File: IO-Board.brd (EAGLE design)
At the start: 160 x 100 mm, 299 parts, among them IC1 PCF8574P, IC2 PCF8574P, IC3 PCF8574P, IC3_INT TPPAD1-13, IC4 PCF8574P, IC4_INT TPPAD1-13, J1.1 TPPAD1-13, J1.2 TPPAD1-13, J1.3 TPPAD1-13, J1.4 TPPAD1-13, J1.5 TPPAD1-13, J1.6 TPPAD1-13, J1.7 TPPAD1-13, J1.8 TPPAD1-13, J2.1 TPPAD1-13, J2.2 TPPAD1-13, J2.3 TPPAD1-13, J2.4 TPPAD1-13, J2.5 TPPAD1-13, J2.6 TPPAD1-13, J2.7 TPPAD1-13, J2.8 TPPAD1-13, J3.1 TPPAD1-13, J3.2 TPPAD1-13, J3.3 TPPAD1-13, J3.4 TPPAD1-13, J3.5 TPPAD1-13, J3.6 TPPAD1-13, J3.7 TPPAD1-13, J3.8 TPPAD1-13, J4.1 TPPAD1-13, J4.2 TPPAD1-13, J4.3 TPPAD1-13, J4.4 TPPAD1-13, J4.5 TPPAD1-13, J4.6 TPPAD1-13, J4.7 TPPAD1-13, J4.8 TPPAD1-13, J5 J7MM, T1 BC337-25, T10 BC337-25, T11 BC337-25, T12 BC337-25, T13 BC337-25, T14 BC337-25, T15 BC337-25, T16 BC337-25, T2 BC337-25, T3 BC337-25, T4 BC337-25, T5 BC337-25, T6 BC337-25, T7 BC337-25, T8 BC337-25, T9 BC337-25

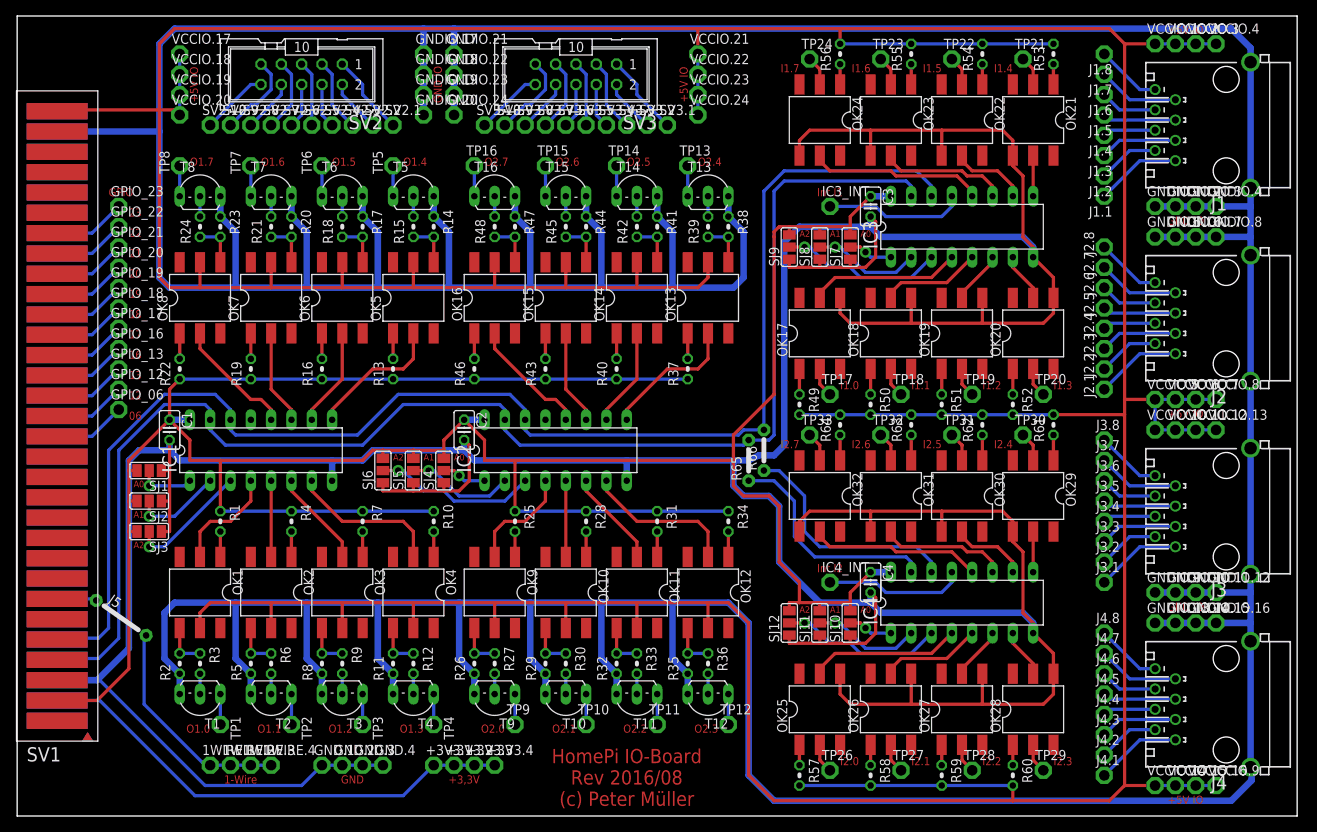
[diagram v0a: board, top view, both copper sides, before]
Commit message: IO-Board und IO-Board-2 Anpassungen
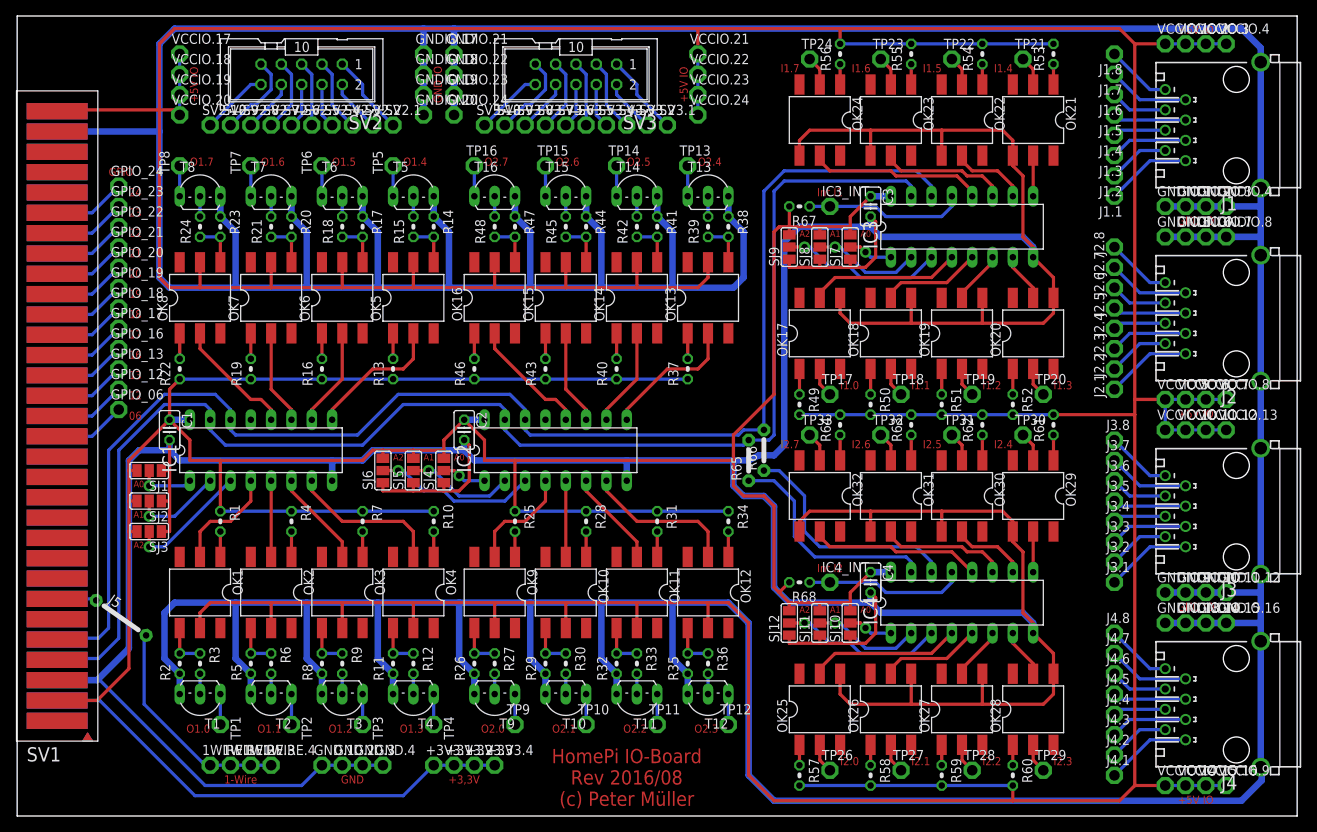
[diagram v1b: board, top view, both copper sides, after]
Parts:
- added GPIO_24: TPPAD1-13, testpad:P1-13
- added R67, R68: 10k, rcl:0204V
- moved GNDIO.10 1.27 mm to (146.1, 27.9)
- moved GNDIO.11 1.27 mm to (148.6, 27.9)
- moved GNDIO.14 1.27 mm to (146.1, 24.1)
- moved GNDIO.15 1.27 mm to (148.6, 24.1)
- moved GNDIO.2 1.27 mm to (146.1, 76.2)
- moved GNDIO.3 1.27 mm to (148.6, 76.2)
- moved GNDIO.6 1.27 mm to (146.1, 72.4)
- moved GNDIO.7 1.27 mm to (148.6, 72.4)
- moved J1 1.27 mm to (152.4, 86.4)
- moved J1.1 1.27 mm to (137.2, 77.5)
- moved J1.2 1.27 mm to (137.2, 80.0)
- moved J1.3 1.27 mm to (137.2, 82.5)
- moved J1.4 1.27 mm to (137.2, 85.1)
- moved J1.5 1.27 mm to (137.2, 87.6)
- moved J1.6 1.27 mm to (137.2, 90.2)
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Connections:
- new net N$177: GPIO_24.TP, SV1.26, SV1.26T
- net +3V3: now also R67.2, R68.2
- net N$106: now also R67.1
- net N$126: now also R68.1
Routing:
- net N$177: track 0.00 -> 9.08 mm
- net VCCIO: track 677.9 -> 681.7 mm
- net +3V3: track 424.9 -> 428.4 mm
- net N$126: track 17.6 -> 20.1 mm
- net N$106: track 17.6 -> 20.1 mm
- net GNDIO: track 767.1 -> 769.6 mm
- net GND: track 553.8 -> 555.7 mm
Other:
- board text added: "24"
